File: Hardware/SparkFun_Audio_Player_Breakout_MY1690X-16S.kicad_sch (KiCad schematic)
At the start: 42 parts, among them J1 3.5mm TRRS, J2 Conn_01x03, J3 Conn_01x02, J4 USB_C_Receptacle, J5 Conn_01x06, J6 microSD, Q1 BSS138, U2 MY1690X-16S

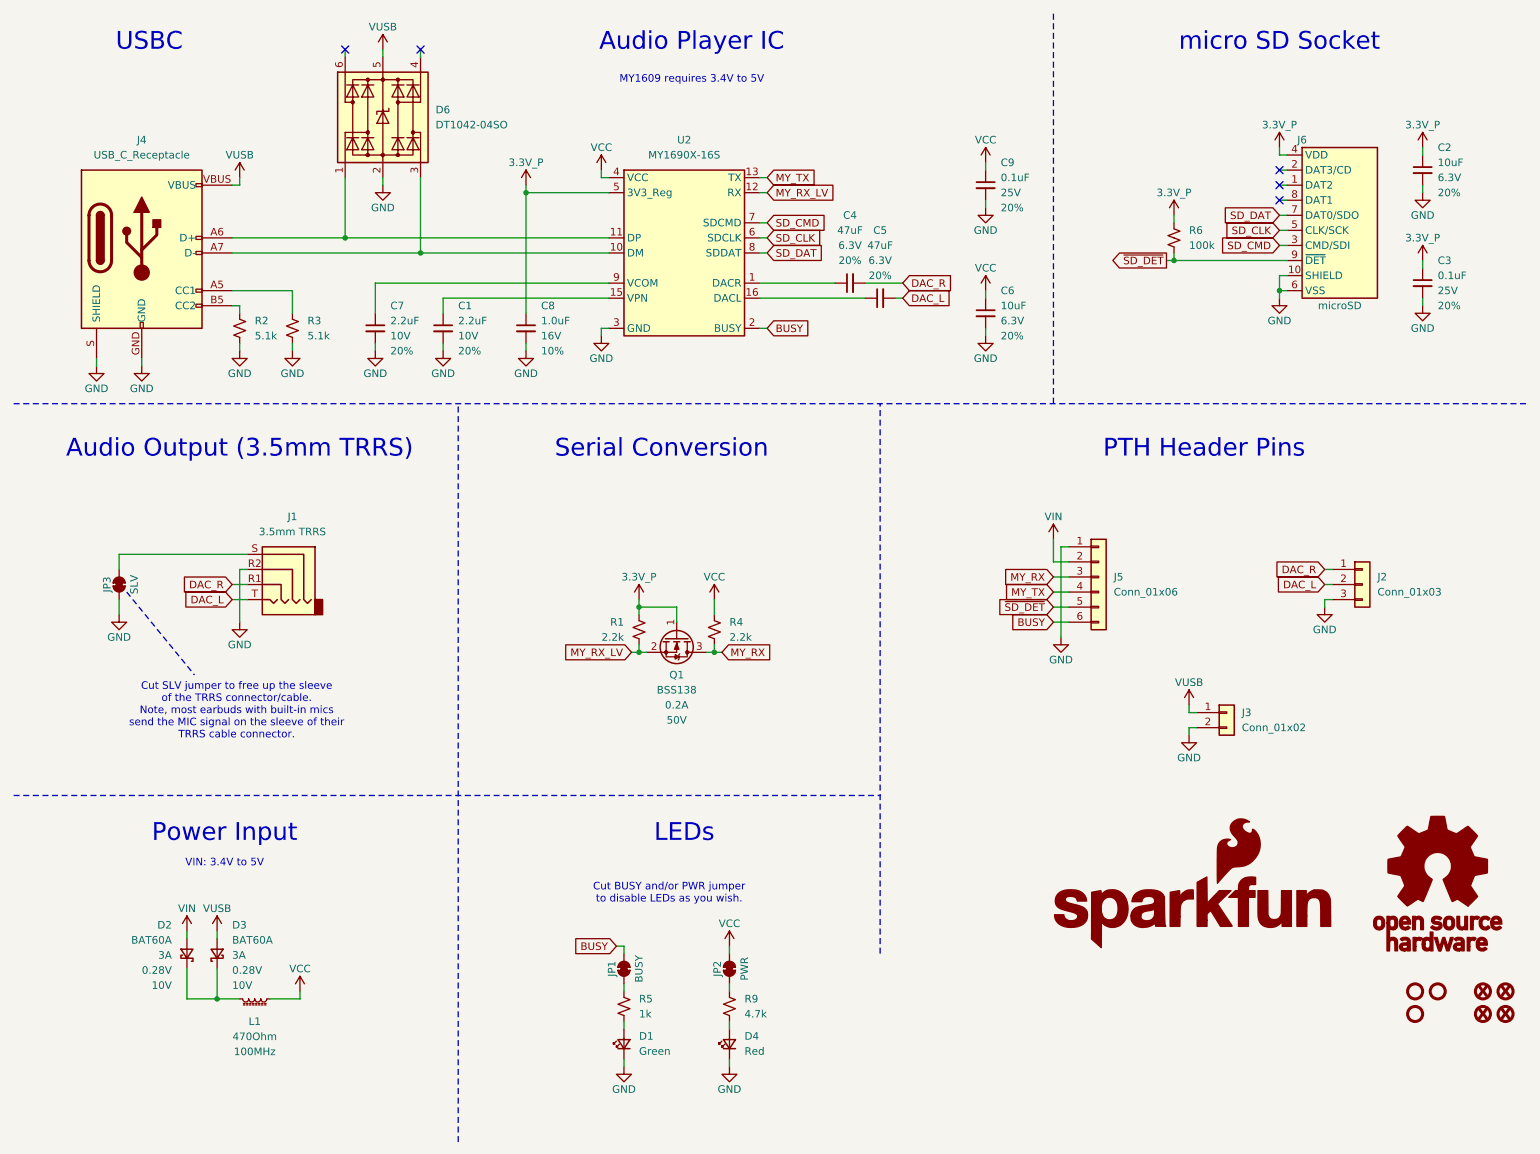
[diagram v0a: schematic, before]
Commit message: USB trace tweaks
-added USB trace calculations to SCH
-general sch cleanup and spacing
-adjusted USB data traces from 10mils to 9.7mils
-adjusted USB data traces routing for proper 7mil gap
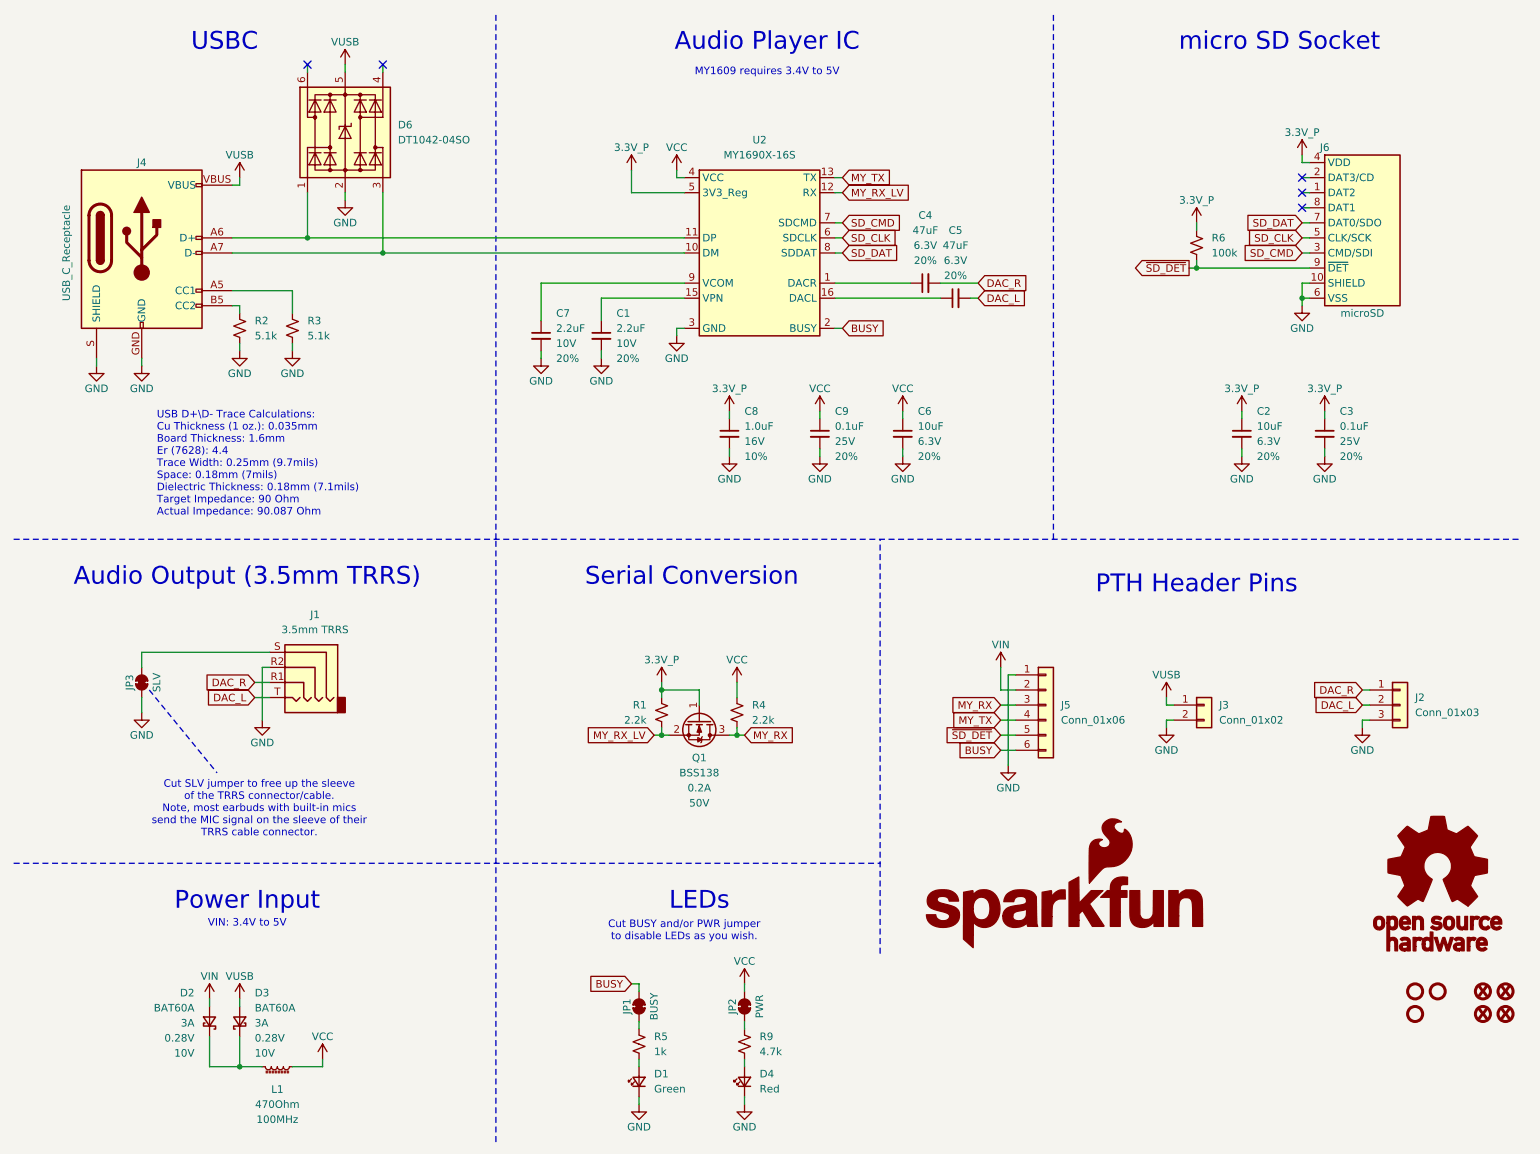
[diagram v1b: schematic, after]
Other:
- note added: "USB D+\D- Trace Calculations: Cu Thickness (1 oz.): 0.035mm Board Thickness: 1.6mm Er (7628): 4.4 Trace Width: 0.25mm (9.7mils) Space: 0.18mm (7mils) Dielectric Thickness: 0.18mm (7.1mils) Target Impedance: 90 Ohm Actual Impedance: 90.087 Ohm"
- moved on the sheet: C1, C2, C3, C4, C5, C6, C7, C8, C9, D1, D2, D3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

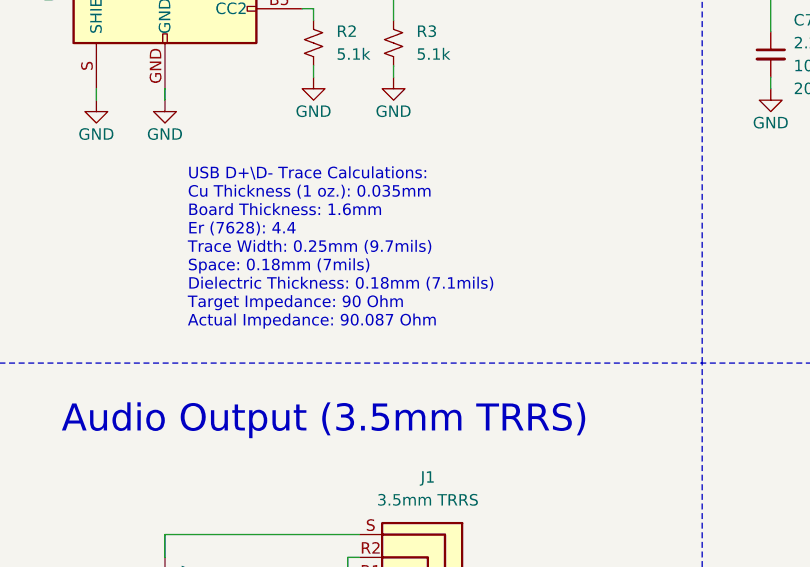
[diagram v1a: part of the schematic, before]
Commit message: corrected USB trace width calcs
-Prepeg is actually 8.28mils, not 7.1, according to Fab houses specs.
-adjusted calcs/traces/gaps
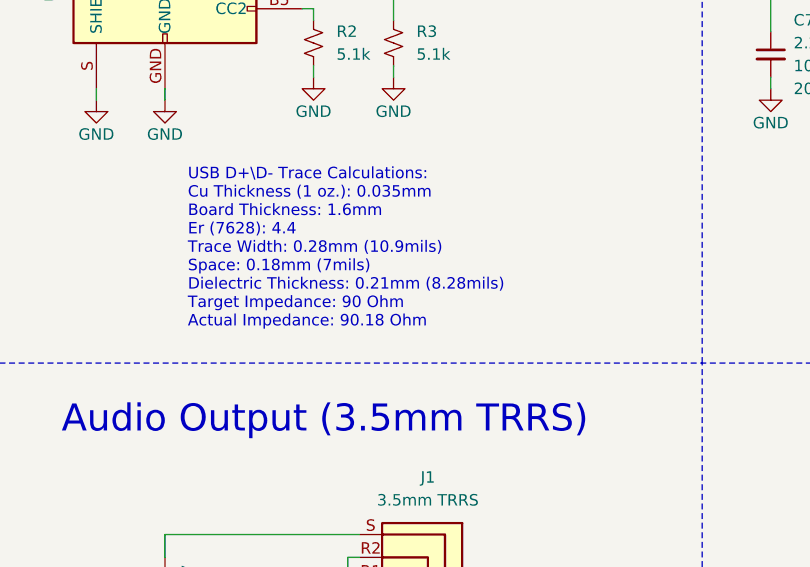
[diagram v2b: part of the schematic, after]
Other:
- note added: "USB D+\D- Trace Calculations: Cu Thickness (1 oz.): 0.035mm Board Thickness: 1.6mm Er (7628): 4.4 Trace Width: 0.28mm (10.9mils) Space: 0.18mm (7mils) Dielectric Thickness: 0.21mm (8.28mils) Target Impedance: 90 Ohm Actual Impedance: 90.18 Ohm"
- note removed: "USB D+\D- Trace Calculations: Cu Thickness (1 oz.): 0.035mm Board Thickness: 1.6mm Er (7628): 4.4 Trace Width: 0.25mm (9.7mils) Space: 0.18mm (7mils) Dielectric Thickness: 0.18mm (7.1mils) Target Impedance: 90 Ohm Actual Impedance: 90.087 Ohm"
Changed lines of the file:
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@@
 		)
 	)
-	(text "USB D+\\D- Trace Calculations:\nCu Thickness (1 oz.): 0.035mm\nBoard Thickness: 1.6mm\nEr (7628): 4.4\nTrace Width: 0.25mm (9.7mils)\nSpace: 0.18mm (7mils)\nDielectric Thickness: 0.18mm (7.1mils)\nTarget Impedance: 90 Ohm\nActual Impedance: 90.087 Ohm\n"
+	(text "USB D+\\D- Trace Calculations:\nCu Thickness (1 oz.): 0.035mm\nBoard Thickness: 1.6mm\nEr (7628): 4.4\nTrace Width: 0.28mm (10.9mils)\nSpace: 0.18mm (7mils)\nDielectric Thickness: 0.21mm (8.28mils)\nTarget Impedance: 90 Ohm\nActual Impedance: 90.18 Ohm\n"
 		(exclude_from_sim no)
 		(at 36.83 88.9 0)
